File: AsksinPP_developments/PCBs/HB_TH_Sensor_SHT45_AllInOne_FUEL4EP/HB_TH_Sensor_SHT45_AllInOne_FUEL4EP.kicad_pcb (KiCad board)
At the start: 2 copper layers, 25 x 75 mm, 41 parts, among them J1 Conn_01x03, J2 FTDI Debuger, J3 ISP Programmer, SW1 Config button, U1 ATmega1284P-AU, U2 TPS61221DCK, U3 SHT45-AD1F-R2

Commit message: PCBs: HB_TH_Sensor_SHT45_AllInOne_FUEL4EP and I2C_Module_SHT45_BME280_FUEL4EP: replacement of SHT45 to type without PTFE filter
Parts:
- U3: value SHT45-AD1F-R2 -> SHT45-AD1B-R2
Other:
- board text added: "Version 1.1 - 12/2023 (KiCAD 6)"
- board text removed: "Version 1.0 - 12/2023 (KiCAD 6)"
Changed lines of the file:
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@@
     (title "HB_TH_Sensor_SHT45_AllInOne_FUEL4EP")
     (date "2023-12-15")
-    (rev "1.0")
+    (rev "1.1")
     (company "FUEL4EP")
   )
@@
   (net 54 "/ANT")
   (net 55 "/CTS")
-  (net 56 "Net-(U1-Pad29)")
-  (net 57 "Net-(R2-Pad2)")
+  (net 56 "Net-(C2-Pad2)")
+  (net 57 "Net-(C8-Pad1)")
   (footprint "LED_SMD:LED_0402_1005Metric" (layer "F.Cu")
     (at 8.128 -32.766 -90)
@@
       (net 1 "GND") (pintype "passive"))
     (pad "2" smd roundrect (at 0.48 0) (size 0.56 0.62) (layers "F.Cu" "F.Paste" "F.Mask") (roundrect_rratio 0.25)
-      (net 56 "Net-(U1-Pad29)") (pintype "passive"))
+      (net 56 "Net-(C2-Pad2)") (pintype "passive"))
     (model "${KICAD6_3DMODEL_DIR}/Capacitor_SMD.3dshapes/C_0402_1005Metric.wrl"
       (offset (xyz 0 0 0))
@@
     (fp_line (start 0.5 0.25) (end -0.5 0.25) (layer "F.Fab") (width 0.1))
     (pad "1" smd roundrect (at -0.48 0) (size 0.56 0.62) (layers "F.Cu" "F.Paste" "F.Mask") (roundrect_rratio 0.25)
-      (net 57 "Net-(R2-Pad2)") (pintype "passive"))
+      (net 57 "Net-(C8-Pad1)") (pintype "passive"))
     (pad "2" smd roundrect (at 0.48 0) (size 0.56 0.62) (layers "F.Cu" "F.Paste" "F.Mask") (roundrect_rratio 0.25)
       (net 1 "GND") (pintype "passive"))
@@
       (net 14 "VCC") (pintype "passive"))
     (pad "2" smd roundrect (at 0.51 0) (size 0.54 0.64) (layers "F.Cu" "F.Paste" "F.Mask") (roundrect_rratio 0.25)
-      (net 57 "Net-(R2-Pad2)") (pintype "passive"))
+      (net 57 "Net-(C8-Pad1)") (pintype "passive"))
     (model "${KICAD6_3DMODEL_DIR}/Resistor_SMD.3dshapes/R_0402_1005Metric.wrl"
       (offset (xyz 0 0 0))
@@
       (net 30 "unconnected-(U1-Pad26)") (pinfunction "PC7") (pintype "bidirectional+no_connect"))
     (pad "27" smd rect (at 5.7 0.8 270) (size 1.5 0.55) (layers "F.Cu" "F.Paste" "F.Mask")
-      (net 57 "Net-(R2-Pad2)") (pinfunction "AVCC") (pintype "power_in"))
+      (net 57 "Net-(C8-Pad1)") (pinfunction "AVCC") (pintype "power_in"))
     (pad "28" smd rect (at 5.7 0 270) (size 1.5 0.55) (layers "F.Cu" "F.Paste" "F.Mask")
       (net 1 "GND") (pinfunction "GND") (pintype "passive"))
     (pad "29" smd rect (at 5.7 -0.8 270) (size 1.5 0.55) (layers "F.Cu" "F.Paste" "F.Mask")
-      (net 56 "Net-(U1-Pad29)") (pinfunction "AREF") (pintype "passive"))
+      (net 56 "Net-(C2-Pad2)") (pinfunction "AREF") (pintype "passive"))
     (pad "30" smd rect (at 5.7 -1.6 270) (size 1.5 0.55) (layers "F.Cu" "F.Paste" "F.Mask")
       (net 31 "unconnected-(U1-Pad30)") (pinfunction "PA7") (pintype "bidirectional+no_connect"))
@@
     (property "Sheetfile" "HB_TH_Sensor_SHT45_AllInOne_FUEL4EP.kicad_sch")
     (property "Sheetname" "")
-    (attr exclude_from_pos_files exclude_from_bom)
+    (attr exclude_from_pos_files)
     (fp_text reference "H4" (at 0 2.032) (layer "F.SilkS")
       (effects (font (size 0.2 0.2) (thickness 0.15)))
@@
     (property "Sheetfile" "HB_TH_Sensor_SHT45_AllInOne_FUEL4EP.kicad_sch")
     (property "Sheetname" "")
-    (attr exclude_from_pos_files exclude_from_bom)
+    (attr exclude_from_pos_files)
     (fp_text reference "H3" (at 0 -1.889) (layer "F.SilkS")
       (effects (font (size 0.2 0.2) (thickness 0.15)))
@@
     (property "Sheetfile" "HB_TH_Sensor_SHT45_AllInOne_FUEL4EP.kicad_sch")
     (property "Sheetname" "")
-    (attr exclude_from_pos_files exclude_from_bom)
+    (attr exclude_from_pos_files)
     (fp_text reference "JP1" (at -0.635 -1.524) (layer "F.SilkS")
       (effects (font (size 0.2 0.2) (thickness 0.05)))
@@
     (property "Sheetfile" "HB_TH_Sensor_SHT45_AllInOne_FUEL4EP.kicad_sch")
     (property "Sheetname" "")
-    (attr exclude_from_pos_files exclude_from_bom)
+    (attr exclude_from_pos_files)
     (fp_text reference "H1" (at -1.997 -0.254) (layer "F.SilkS")
       (effects (font (size 0.2 0.2) (thickness 0.15)))
@@
     (at 1.74 -14.214)
     (descr "Consumer SHT4x Digital and Analog")
-    (property "LCSC" "C5360602")
+    (property "LCSC" "C5221601")
     (property "Sheetfile" "HB_TH_Sensor_SHT45_AllInOne_FUEL4EP.kicad_sch")
     (property "Sheetname" "")
@@
       (effects (font (size 0.2 0.2) (thickness 0.15)))
     )
-    (fp_text value "SHT45-AD1F-R2" (at -0.216 1.387) (layer "F.Fab")
+    (fp_text value "SHT45-AD1B-R2" (at -0.216 1.387) (layer "F.Fab")
       (effects (font (size 0.2 0.2) (thickness 0.15)))
     )
@@
     (property "Sheetfile" "HB_TH_Sensor_SHT45_AllInOne_FUEL4EP.kicad_sch")
     (property "Sheetname" "")
-    (attr exclude_from_pos_files exclude_from_bom)
+    (attr exclude_from_pos_files)
     (fp_text reference "H2" (at 0 -1.905) (layer "F.SilkS")
       (effects (font (size 0.2 0.2) (thickness 0.15)))
@@
     (property "Sheetfile" "HB_TH_Sensor_SHT45_AllInOne_FUEL4EP.kicad_sch")
     (property "Sheetname" "")
-    (attr through_hole exclude_from_pos_files exclude_from_bom)
+    (attr through_hole exclude_from_pos_files)
     (fp_text reference "J1" (at 0 1.996) (layer "B.SilkS")
       (effects (font (size 0.2 0.2) (thickness 0.15)) (justify mirror))
@@
     (property "Sheetname" "")
     (property "TYPE" "0")
-    (attr through_hole exclude_from_pos_files exclude_from_bom)
+    (attr through_hole exclude_from_pos_files)
     (fp_text reference "J3" (at 0 2.032) (layer "B.SilkS")
       (effects (font (size 0.2 0.2) (thickness 0.15)) (justify mirror))
@@
     (property "Sheetname" "")
     (property "TYPE" "0")
-    (attr through_hole exclude_from_pos_files exclude_from_bom)
+    (attr through_hole exclude_from_pos_files)
     (fp_text reference "J2" (at -0.077 2.032) (layer "B.SilkS")
       (effects (font (size 0.2 0.2) (thickness 0.15)) (justify mirror))
@@
   (gr_line (start 0 -12.319) (end 0 -16.129) (layer "Edge.Cuts") (width 0.038099))
   (gr_line (start 0 -12.319) (end 2.667 -12.319) (layer "Edge.Cuts") (width 0.038099))
-  (gr_text "Version 1.0 - 12/2023 (KiCAD 6)\n" (at 6.223 -41.148 90) (layer "B.SilkS")
+  (gr_text "Version 1.1 - 12/2023 (KiCAD 6)\n" (at 6.223 -41.148 90) (layer "B.SilkS")
     (effects (font (size 1.2 1.2) (thickness 0.2)) (justify left mirror))
   )

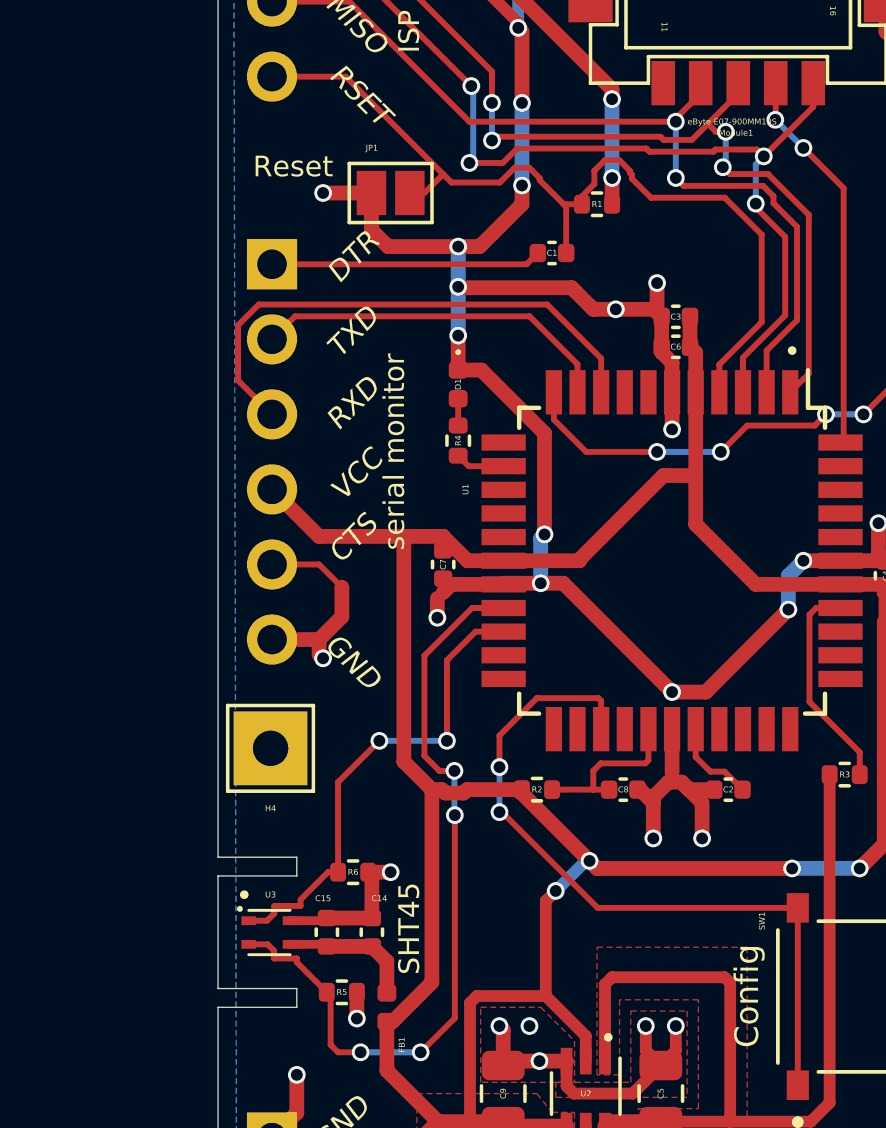
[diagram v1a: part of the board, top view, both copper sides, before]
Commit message: PCBs: HB_TH_Sensor_SHT45_AllInOne_FUEL4EP and HB-UNI-SEN-BATT_ATMega1284P_E07-900MM10S_FUEL4EP: fix of wrong LCSC part numbers
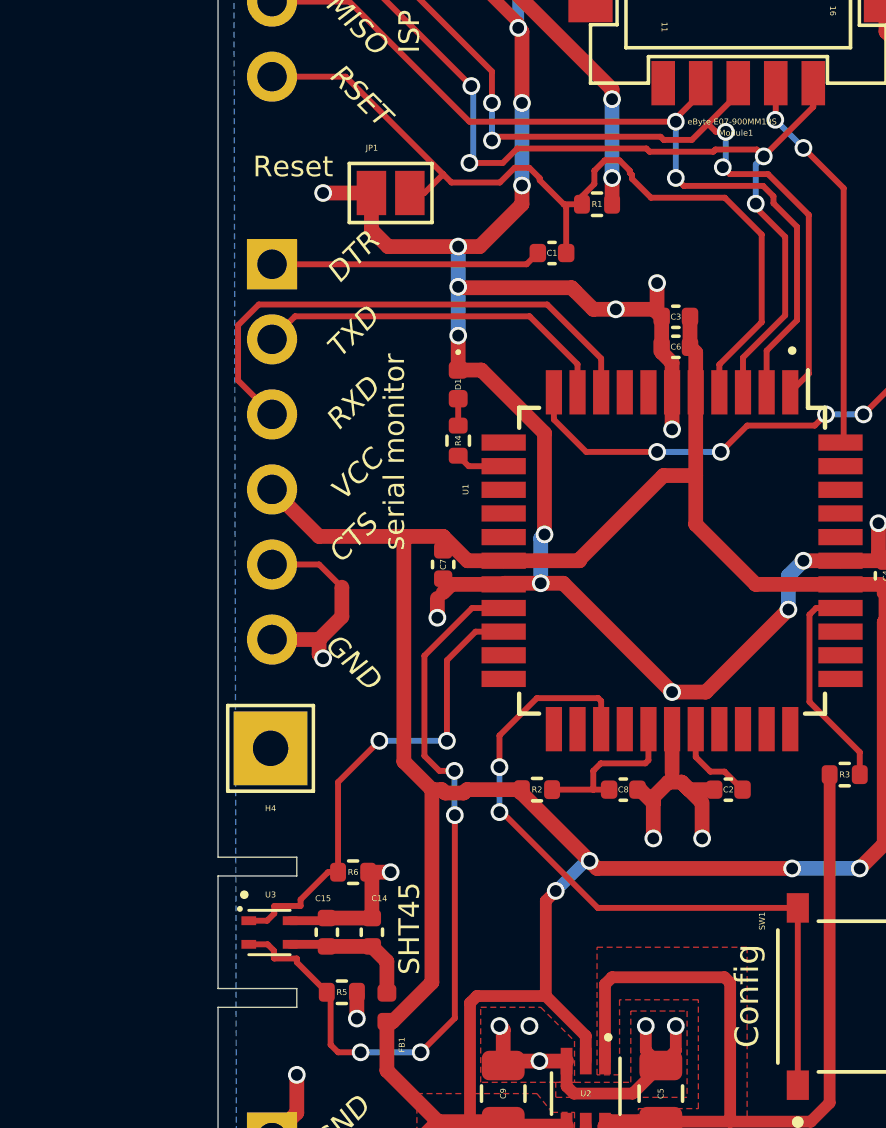
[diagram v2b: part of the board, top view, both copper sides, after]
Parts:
- D1: value LED red 3mm -> LED red 0402
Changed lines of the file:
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@@
     (descr "LED SMD 0402 (1005 Metric), square (rectangular) end terminal, IPC_7351 nominal, (Body size source: http://www.tortai-tech.com/upload/download/2011102023233369053.pdf), generated with kicad-footprint-generator")
     (tags "LED")
-    (property "LCSC" "C84256")
+    (property "LCSC" "C273598")
     (property "Sheetfile" "HB_TH_Sensor_SHT45_AllInOne_FUEL4EP.kicad_sch")
     (property "Sheetname" "")
-    (property "TYPE" "LED_0805")
+    (property "TYPE" "0402")
     (attr smd)
     (fp_text reference "D1" (at 0 0 90) (layer "F.SilkS")
       (effects (font (size 0.2 0.2) (thickness 0.15)))
     )
-    (fp_text value "LED red 3mm" (at 0 0.762 90) (layer "F.Fab")
+    (fp_text value "LED red 0402" (at 0 0.762 90) (layer "F.Fab")
       (effects (font (size 0.2 0.2) (thickness 0.15)))
     )
@@
     (descr "Resistor SMD 0402 (1005 Metric), square (rectangular) end terminal, IPC_7351 nominal, (Body size source: IPC-SM-782 page 72, https://www.pcb-3d.com/wordpress/wp-content/uploads/ipc-sm-782a_amendment_1_and_2.pdf), generated with kicad-footprint-generator")
     (tags "resistor")
-    (property "LCSC" "C17710")
+    (property "LCSC" "C25117")
     (property "Sheetfile" "HB_TH_Sensor_SHT45_AllInOne_FUEL4EP.kicad_sch")
     (property "Sheetname" "")
-    (property "TYPE" "0805")
+    (property "TYPE" "0402")
     (attr smd)
     (fp_text reference "R4" (at 0 0 90) (layer "F.SilkS")
@@
     (descr "Resistor SMD 0402 (1005 Metric), square (rectangular) end terminal, IPC_7351 nominal, (Body size source: IPC-SM-782 page 72, https://www.pcb-3d.com/wordpress/wp-content/uploads/ipc-sm-782a_amendment_1_and_2.pdf), generated with kicad-footprint-generator")
     (tags "resistor")
-    (property "LCSC" "C17733")
+    (property "LCSC" "C25744")
     (property "Sheetfile" "HB_TH_Sensor_SHT45_AllInOne_FUEL4EP.kicad_sch")
     (property "Sheetname" "")
-    (property "TYPE" "0805")
+    (property "TYPE" "0402")
     (attr smd)
     (fp_text reference "R1" (at 0 0) (layer "F.SilkS")
@@
   (segment (start 8.128 -33.251) (end 8.913 -33.251) (width 0.5) (layer "F.Cu") (net 1))
   (segment (start 19.304 -55.598) (end 19.205 -55.499) (width 0.5) (layer "F.Cu") (net 1))
-  (segment (start 3.593 -14.614) (end 3.683 -14.704) (width 0.3) (layer "F.Cu") (net 1))
   (segment (start 10.922 -26.035) (end 9.705 -26.035) (width 0.5) (layer "F.Cu") (net 1))
   (segment (start 9.652 -10.922) (end 9.525 -11.049) (width 0.5) (layer "F.Cu") (net 1))
@@
   (segment (start 5.207 -13.744) (end 5.715 -13.236) (width 0.5) (layer "F.Cu") (net 7))
   (segment (start 5.715 -13.236) (end 5.715 -12.169) (width 0.5) (layer "F.Cu") (net 7))
-  (segment (start 3.613 -13.814) (end 3.683 -13.744) (width 0.3) (layer "F.Cu") (net 7))
   (segment (start 5.207 -13.744) (end 3.683 -13.744) (width 0.5) (layer "F.Cu") (net 7))
   (segment (start 16.5815 -41.5845) (end 16.036501 -41.039501) (width 0.2) (layer "F.Cu") (net 11))
@@
   (segment (start 14.011501 -39.724611) (end 14.011501 -39.851611) (width 0.2) (layer "F.Cu") (net 24))
   (segment (start 13.585322 -40.3485) (end 13.088678 -40.3485) (width 0.2) (layer "F.Cu") (net 24))
-  (segment (start 10.8865 -39.674612) (end 11.501056 -39.060056) (width 0.2) (layer "F.Cu") (net 24))
+  (segment (start 10.8865 -39.674612) (end 11.699112 -38.862) (width 0.2) (layer "F.Cu") (net 24))
   (segment (start 4.318 -43.18) (end 7.62 -39.878) (width 0.2) (layer "F.Cu") (net 24))
   (segment (start 7.62 -39.878) (end 7.900389 -39.597611) (width 0.2) (layer "F.Cu") (net 24))
-  (segment (start 11.501056 -39.060056) (end 11.699112 -38.862) (width 0.2) (layer "F.Cu") (net 24))
   (segment (start 11.783 -37.211) (end 11.783 -38.778112) (width 0.2) (layer "F.Cu") (net 24))
   (segment (start 18.4 -34.870183) (end 18.4 -37.834817) (width 0.2) (layer "F.Cu") (net 24))

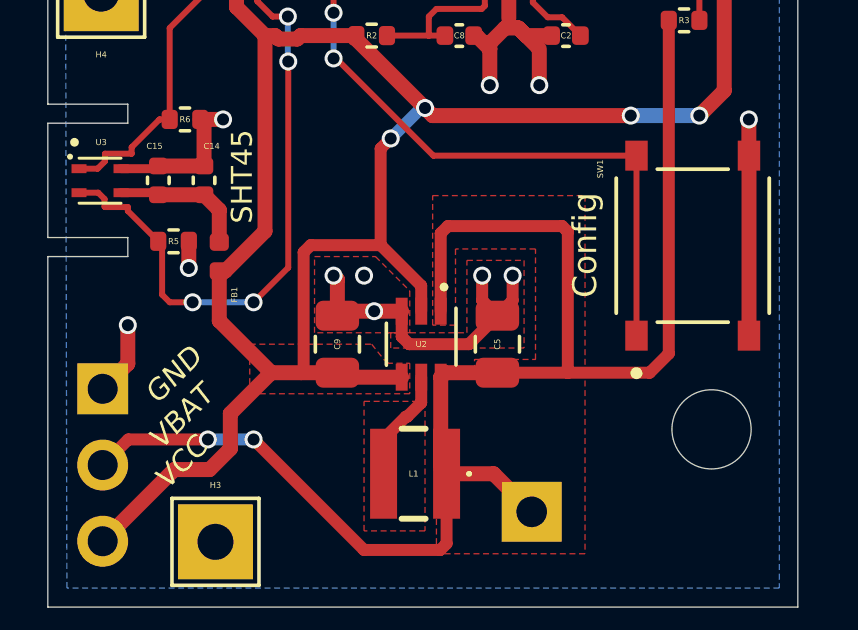
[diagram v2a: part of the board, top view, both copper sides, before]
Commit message: PCBs: HB_TH_Sensor_SHT45_AllInOne_FUEL4EP (updates), added HB_Stamp_ATMega1284P_FUEL4EP and I2C_Module_SHT45_BME280_small_FUEL4EP
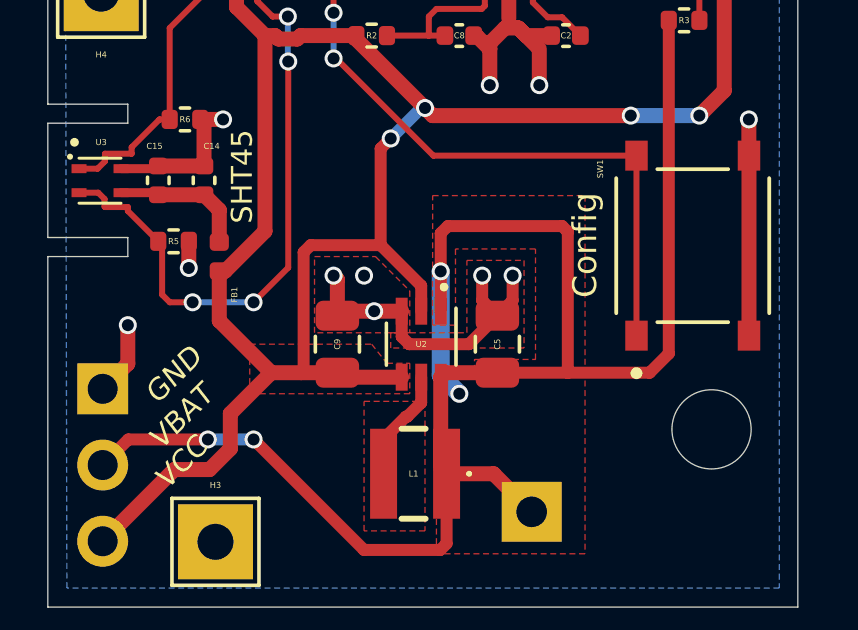
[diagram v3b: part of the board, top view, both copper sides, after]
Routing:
- net /plusBAT: track 52.9 -> 57.2 mm, vias 2 -> 4
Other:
- board text added: "Version 1.2 - 01/2024 (KiCAD 6)"
- board text removed: "Version 1.1 - 12/2023 (KiCAD 6)"
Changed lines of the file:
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@@
   (title_block
     (title "HB_TH_Sensor_SHT45_AllInOne_FUEL4EP")
-    (date "2023-12-15")
-    (rev "1.1")
+    (date "2024-01-12")
+    (rev "1.2")
     (company "FUEL4EP")
   )
@@
     (property "Sheetname" "")
     (property "TYPE" "10x10mm")
-    (attr smd)
+    (attr smd exclude_from_pos_files)
     (fp_text reference "Module1" (at 11.684 5.08 180) (layer "F.SilkS")
       (effects (font (size 0.2 0.2) (thickness 0.15)))
@@
     (descr "R-PDSO-G6, http://www.ti.com/lit/ds/slis144b/slis144b.pdf")
     (tags "R-PDSO-G6 SC-70-6")
-    (property "LCSC" "C37055")
+    (property "LCSC" "C2865756")
     (property "Sheetfile" "HB_TH_Sensor_SHT45_AllInOne_FUEL4EP.kicad_sch")
     (property "Sheetname" "")
@@
   (gr_line (start 0 -12.319) (end 0 -16.129) (layer "Edge.Cuts") (width 0.038099))
   (gr_line (start 0 -12.319) (end 2.667 -12.319) (layer "Edge.Cuts") (width 0.038099))
-  (gr_text "Version 1.1 - 12/2023 (KiCAD 6)\n" (at 6.223 -41.148 90) (layer "B.SilkS")
+  (gr_text "Version 1.2 - 01/2024 (KiCAD 6)\n" (at 6.223 -41.148 90) (layer "B.SilkS")
     (effects (font (size 1.2 1.2) (thickness 0.2)) (justify left mirror))
   )
@@
   (segment (start 17.333 -7.813) (end 14.986 -7.813) (width 0.4) (layer "F.Cu") (net 17))
   (segment (start 17.145 -12.7) (end 17.333 -12.512) (width 0.4) (layer "F.Cu") (net 17))
+  (segment (start 13.096 -11.191) (end 13.096 -12.461) (width 0.4) (layer "F.Cu") (net 17))
   (segment (start 6.858 -5.588) (end 10.541 -1.905) (width 0.4) (layer "F.Cu") (net 17))
   (segment (start 13.096 -7.663) (end 13.096 -4.641) (width 0.5) (layer "F.Cu") (net 17))
@@
   (segment (start 10.541 -1.905) (end 13.081 -1.905) (width 0.4) (layer "F.Cu") (net 17))
   (segment (start 1.828 -4.735) (end 2.681 -5.588) (width 0.4) (layer "F.Cu") (net 17))
-  (segment (start 13.096 -9.863) (end 13.096 -12.461) (width 0.4) (layer "F.Cu") (net 17))
+  (segment (start 13.096 -9.863) (end 13.096 -11.191) (width 0.4) (layer "F.Cu") (net 17))
   (segment (start 13.081 -1.905) (end 13.292 -2.116) (width 0.4) (layer "F.Cu") (net 17))
   (segment (start 13.096 -12.461) (end 13.335 -12.7) (width 0.4) (layer "F.Cu") (net 17))
   (segment (start 13.292 -4.445) (end 14.859 -4.445) (width 0.5) (layer "F.Cu") (net 17))
   (segment (start 20.062505 -7.813) (end 17.333 -7.813) (width 0.4) (layer "F.Cu") (net 17))
+  (via (at 13.716 -7.112) (size 0.6) (drill 0.4) (layers "F.Cu" "B.Cu") (free) (net 17))
   (via (at 5.334 -5.588) (size 0.6) (drill 0.4) (layers "F.Cu" "B.Cu") (net 17))
+  (via (at 13.096 -11.191) (size 0.6) (drill 0.4) (layers "F.Cu" "B.Cu") (net 17))
   (via (at 6.858 -5.588) (size 0.6) (drill 0.4) (layers "F.Cu" "B.Cu") (net 17))
+  (segment (start 13.096 -11.191) (end 13.096 -7.732) (width 0.6) (layer "B.Cu") (net 17))
   (segment (start 6.858 -5.588) (end 5.334 -5.588) (width 0.4) (layer "B.Cu") (net 17))
+  (segment (start 13.096 -7.732) (end 13.716 -7.112) (width 0.6) (layer "B.Cu") (net 17))
   (segment (start 12.867 -22.147) (end 10.792 -22.147) (width 0.2) (layer "F.Cu") (net 22))
   (segment (start 10.792 -22.147) (end 9.525 -20.88) (width 0.2) (layer "F.Cu") (net 22))
